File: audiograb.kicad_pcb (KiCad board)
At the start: 4 copper layers, 167 x 69.7 mm, 113 parts, among them IC1 USB2244I-AEZG-06, J1 USB_C_Receptacle_USB2.0_16P, J10 TestPoint, J11 TestPoint, J12 TestPoint, J13 TestPoint, J14 TestPoint, J15 F32Q-1A7H1-11022, J16 MEM2075-00-140-01-A, J17 5V_out, J18 3V7_in, J19 3V3_in, J2 SAM10346-ND, J3 Conn_02x20_Odd_Even, J4 EMPCB.SMAFSTJ.B.HT, J5 EMPCB.SMAFSTJ.B.HT, J6 TestPoint, J7 TestPoint, J8 TestPoint, J9 TestPoint, M1 ComputeModule5-CM5, P1 SF72S006VBAR2500, Q1 Q_PMOS_GSD, SW1 1825910-6, U1 RC7620_1104625, U10 CD4043BDR, U11 TPS22919DCKR, U12 IP4220CZ6F, U2 NX3008NBKW_115, U3 NX3008NBKW_115, U4 NX3008NBKW_115, U5 NX3008NBKW_115, U6 NX3008NBKW_115, U7 NX3008NBKW_115, U8 MAX4996LETG_

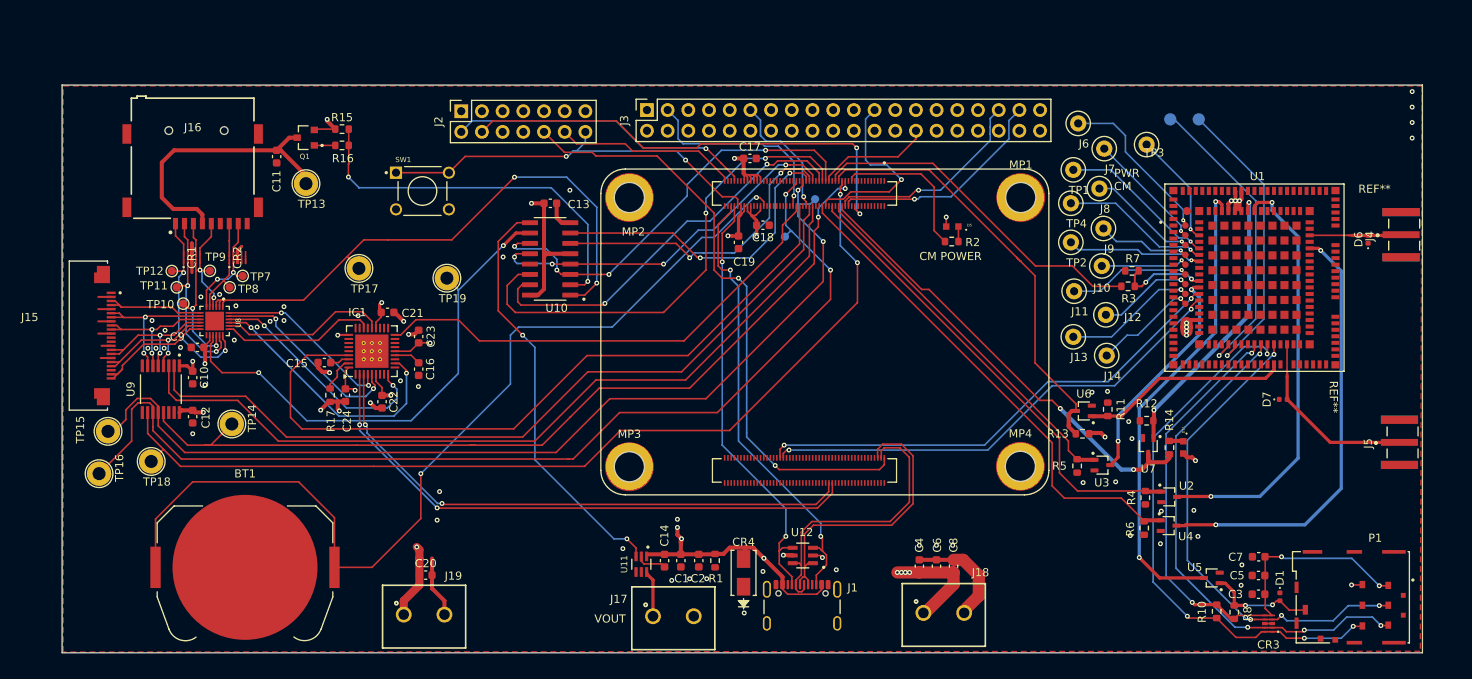
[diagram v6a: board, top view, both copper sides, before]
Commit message: Added thruholes to for antenna and aorund the pcb, and fillements
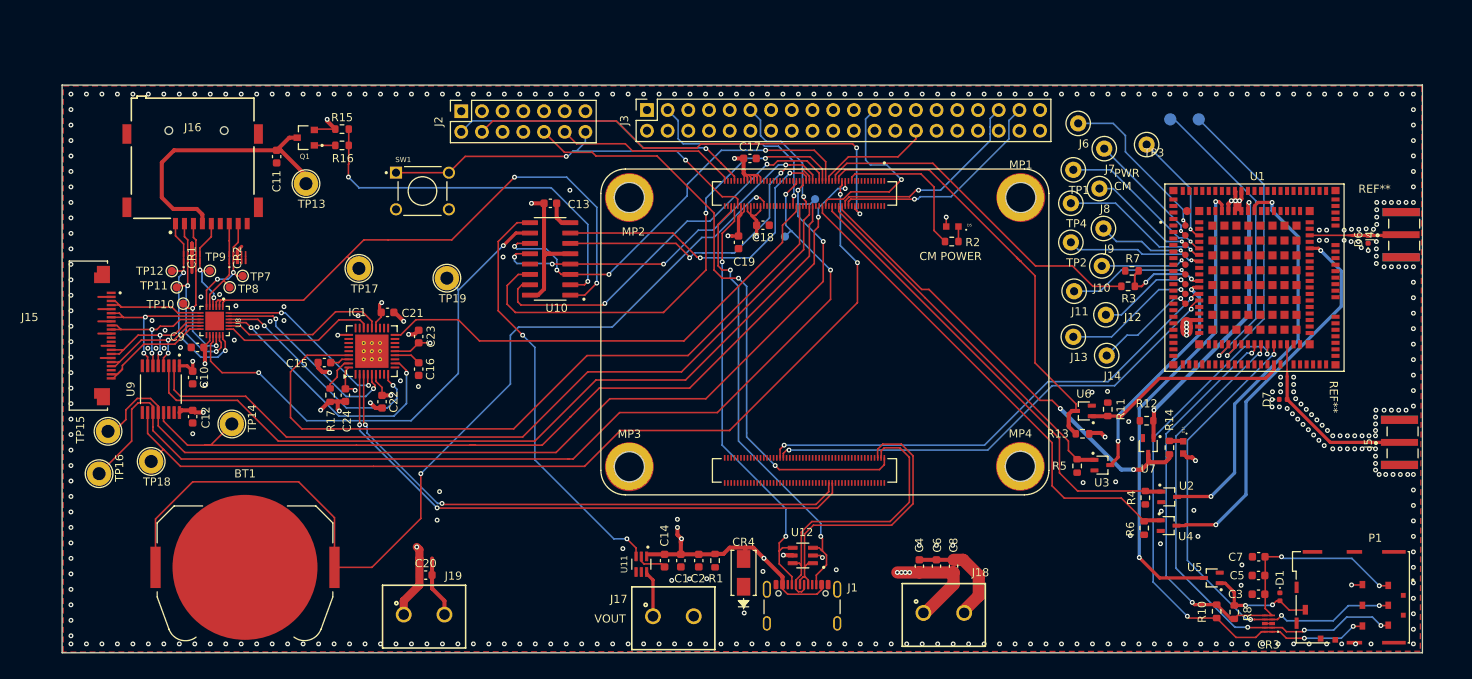
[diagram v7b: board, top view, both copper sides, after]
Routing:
- net /modem/1V8_BOOT_MODE: track 53.8 -> 47.4 mm
- net /modem/1V8_POWER_ON_N: track 52.5 -> 49.0 mm
- net +3V3: track 293.4 -> 292.4 mm
- net GND: vias 55 -> 377
- net (no net): vias 4 -> 0
